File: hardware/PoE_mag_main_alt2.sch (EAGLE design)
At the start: 121 parts, among them IC1 LD1117S33TR, IC10 PCA9517A, IC2 DS1338, IC3 74LVC1T45SOT23-HAND, IC4 ATMEGA1284, IC5 MCP2200, IC6 TSR 1-2450, IC7 74LVC1T45SOT23-HAND, IC8 74LVC1T45SOT23-HAND, IC9 74LVC1T45SOT23-HAND, Q1 BSS138, Q3 BUK98150-55A, X1 PWR, X2 JTAG, X3 USB, X4 CONN-SMATHD, X5 UFL, X6 MICRO-SD-SOCKETHIROSE-DM3D, X7 RJ45, X8 RJ11, X9 22-23-2021, Y1 32k768, Y2 16MHz, Y3 12MHz

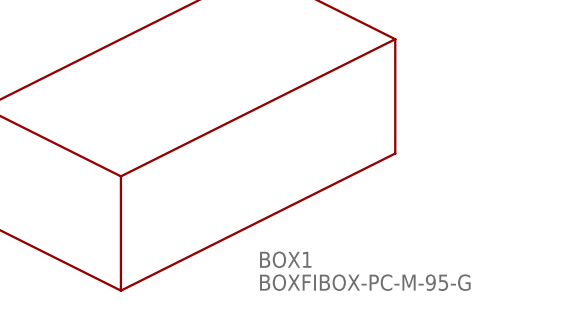
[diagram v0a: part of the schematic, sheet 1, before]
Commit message: Update enclosure outline
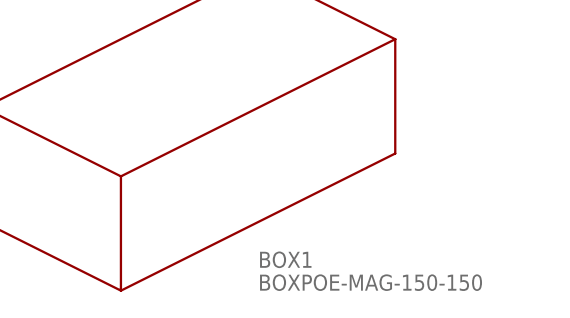
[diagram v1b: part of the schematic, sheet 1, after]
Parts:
- BOX1: value BOXFIBOX-PC-M-95-G -> BOXPOE-MAG-150-150; device fibox:BOXFIBOX-PC-M-95-G -> fibox:BOXPOE-MAG-150-150
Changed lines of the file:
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@@
 <grid distance="0.1" unitdist="inch" unit="inch" style="lines" multiple="1" display="no" altdistance="0.01" altunitdist="inch" altunit="inch"/>
 <layers>
-<layer number="1" name="Top" color="4" fill="1" visible="no" active="no"/>
-<layer number="2" name="Route2" color="1" fill="3" visible="no" active="no"/>
-<layer number="3" name="Route3" color="4" fill="3" visible="no" active="no"/>
-<layer number="14" name="Route14" color="1" fill="6" visible="no" active="no"/>
-<layer number="15" name="Route15" color="4" fill="6" visible="no" active="no"/>
-<layer number="16" name="Bottom" color="1" fill="1" visible="no" active="no"/>
-<layer number="17" name="Pads" color="2" fill="1" visible="no" active="no"/>
-<layer number="18" name="Vias" color="2" fill="1" visible="no" active="no"/>
-<layer number="19" name="Unrouted" color="6" fill="1" visible="no" active="no"/>
-<layer number="20" name="Dimension" color="15" fill="1" visible="no" active="no"/>
-<layer number="21" name="tPlace" color="7" fill="1" visible="no" active="no"/>
-<layer number="22" name="bPlace" color="7" fill="1" visible="no" active="no"/>
-<layer number="23" name="tOrigins" color="15" fill="1" visible="no" active="no"/>
-<layer number="24" name="bOrigins" color="15" fill="1" visible="no" active="no"/>
-<layer number="25" name="tNames" color="7" fill="1" visible="no" active="no"/>
-<layer number="26" name="bNames" color="7" fill="1" visible="no" active="no"/>
-<layer number="27" name="tValues" color="7" fill="1" visible="no" active="no"/>
-<layer number="28" name="bValues" color="7" fill="1" visible="no" active="no"/>
+<layer number="1" name="Top" color="4" fill="1" visible="yes" active="no"/>
+<layer number="2" name="Route2" color="1" fill="3" visible="yes" active="no"/>
+<layer number="3" name="Route3" color="4" fill="3" visible="yes" active="no"/>
+<layer number="14" name="Route14" color="1" fill="6" visible="yes" active="no"/>
+<layer number="15" name="Route15" color="4" fill="6" visible="yes" active="no"/>
+<layer number="16" name="Bottom" color="1" fill="1" visible="yes" active="no"/>
+<layer number="17" name="Pads" color="2" fill="1" visible="yes" active="no"/>
+<layer number="18" name="Vias" color="2" fill="1" visible="yes" active="no"/>
+<layer number="19" name="Unrouted" color="6" fill="1" visible="yes" active="no"/>
+<layer number="20" name="Dimension" color="14" fill="1" visible="yes" active="no"/>
+<layer number="21" name="tPlace" color="7" fill="1" visible="yes" active="no"/>
+<layer number="22" name="bPlace" color="7" fill="1" visible="yes" active="no"/>
+<layer number="23" name="tOrigins" color="15" fill="1" visible="yes" active="no"/>
+<layer number="24" name="bOrigins" color="15" fill="1" visible="yes" active="no"/>
+<layer number="25" name="tNames" color="7" fill="1" visible="yes" active="no"/>
+<layer number="26" name="bNames" color="7" fill="1" visible="yes" active="no"/>
+<layer number="27" name="tValues" color="7" fill="1" visible="yes" active="no"/>
+<layer number="28" name="bValues" color="7" fill="1" visible="yes" active="no"/>
 <layer number="29" name="tStop" color="7" fill="3" visible="no" active="no"/>
 <layer number="30" name="bStop" color="7" fill="6" visible="no" active="no"/>
@@
 <layer number="35" name="tGlue" color="7" fill="4" visible="no" active="no"/>
 <layer number="36" name="bGlue" color="7" fill="5" visible="no" active="no"/>
-<layer number="37" name="tTest" color="7" fill="1" visible="no" active="no"/>
-<layer number="38" name="bTest" color="7" fill="1" visible="no" active="no"/>
+<layer number="37" name="tTest" color="7" fill="1" visible="yes" active="no"/>
+<layer number="38" name="bTest" color="7" fill="1" visible="yes" active="no"/>
 <layer number="39" name="tKeepout" color="4" fill="11" visible="no" active="no"/>
 <layer number="40" name="bKeepout" color="1" fill="11" visible="no" active="no"/>
@@
 <layer number="44" name="Drills" color="7" fill="1" visible="no" active="no"/>
 <layer number="45" name="Holes" color="7" fill="1" visible="no" active="no"/>
-<layer number="46" name="Milling" color="3" fill="1" visible="no" active="no"/>
-<layer number="47" name="Measures" color="7" fill="1" visible="no" active="no"/>
-<layer number="48" name="Document" color="7" fill="1" visible="no" active="no"/>
-<layer number="49" name="Reference" color="7" fill="1" visible="no" active="no"/>
-<layer number="50" name="dxf" color="7" fill="1" visible="no" active="no"/>
-<layer number="51" name="tDocu" color="7" fill="1" visible="no" active="no"/>
-<layer number="52" name="bDocu" color="7" fill="1" visible="no" active="no"/>
-<layer number="53" name="tGND_GNDA" color="7" fill="9" visible="no" active="no"/>
-<layer number="54" name="bGND_GNDA" color="1" fill="9" visible="no" active="no"/>
-<layer number="56" name="wert" color="7" fill="1" visible="no" active="no"/>
-<layer number="57" name="tCAD" color="7" fill="1" visible="no" active="no"/>
+<layer number="46" name="Milling" color="3" fill="1" visible="yes" active="no"/>
+<layer number="47" name="Measures" color="7" fill="1" visible="yes" active="no"/>
+<layer number="48" name="Document" color="7" fill="1" visible="yes" active="no"/>
+<layer number="49" name="Reference" color="7" fill="1" visible="yes" active="no"/>
+<layer number="50" name="dxf" color="7" fill="1" visible="yes" active="no"/>
+<layer number="51" name="tDocu" color="7" fill="1" visible="yes" active="no"/>
+<layer number="52" name="bDocu" color="7" fill="1" visible="yes" active="no"/>
+<layer number="53" name="tGND_GNDA" color="7" fill="9" visible="yes" active="no"/>
+<layer number="54" name="bGND_GNDA" color="1" fill="9" visible="yes" active="no"/>
+<layer number="56" name="wert" color="7" fill="1" visible="yes" active="no"/>
+<layer number="57" name="tCAD" color="7" fill="1" visible="yes" active="no"/>
 <layer number="91" name="Nets" color="2" fill="1" visible="yes" active="yes"/>
 <layer number="92" name="Busses" color="1" fill="1" visible="yes" active="yes"/>
@@
 <part name="GND48" library="supply1" deviceset="GND" device=""/>
 <part name="X9" library="con-molex" deviceset="22-23-2021" device=""/>
-<part name="BOX1" library="fibox" deviceset="BOX" device="FIBOX-PC-M-95-G"/>
+<part name="BOX1" library="fibox" deviceset="BOX" device="POE-MAG-150-150" value="BOXPOE-MAG-150-150"/>
 <part name="Q3" library="SteveMarple" deviceset="FET-N-TYPE" device="SOT223-HAND" value="BUK98150-55A"/>
 </parts>

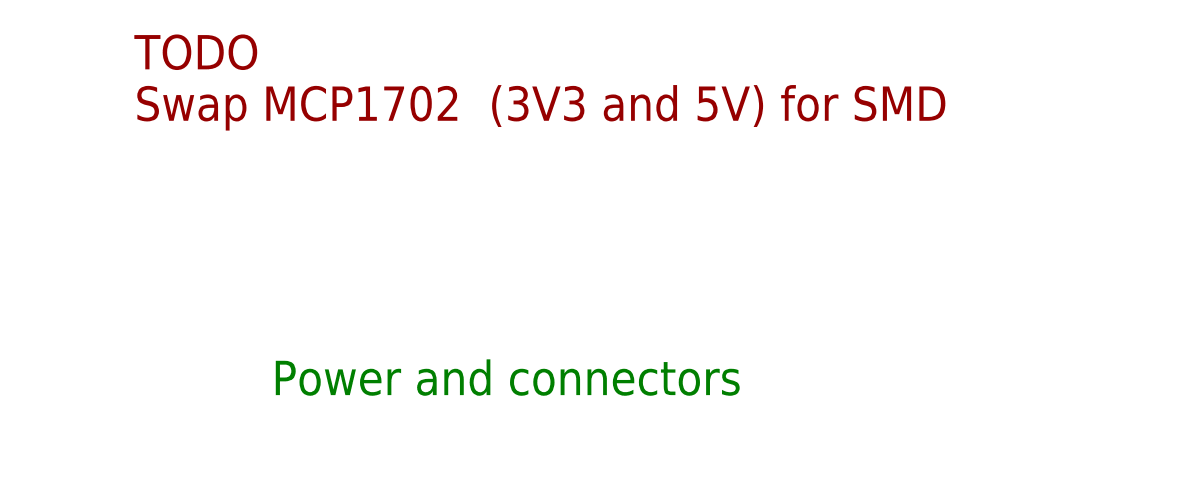
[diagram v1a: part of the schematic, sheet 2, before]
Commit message: Update enclosure restrictions
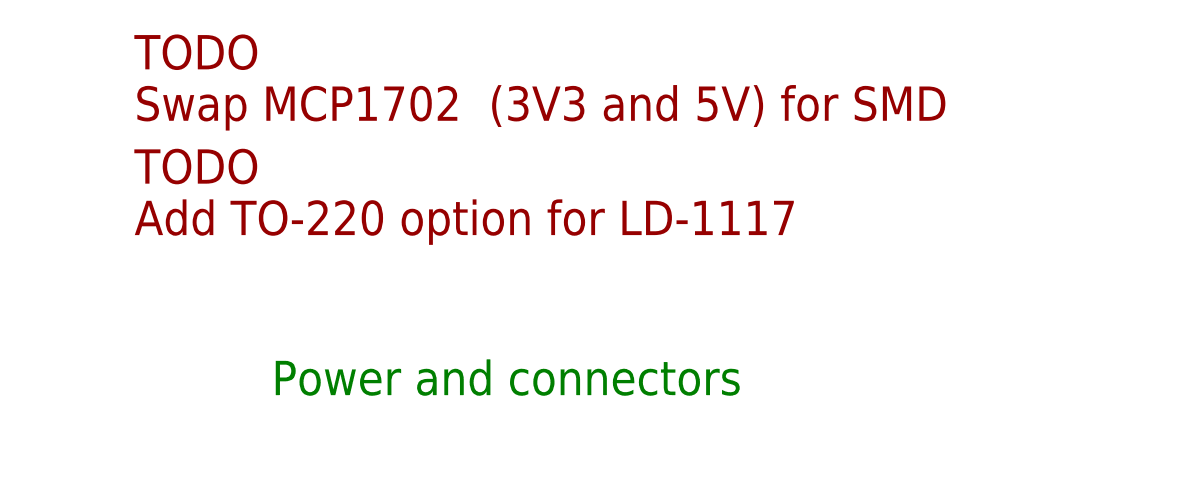
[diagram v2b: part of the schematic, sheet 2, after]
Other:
- note added: "TODO Add TO-220 option for LD-1117"
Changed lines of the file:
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@@
 <text x="-149.86" y="200.66" size="3.81" layer="94">TODO
 Swap MCP1702  (3V3 and 5V) for SMD</text>
+<text x="-149.86" y="187.96" size="3.81" layer="94">TODO
+Add TO-220 option for LD-1117</text>
 </plain>
 <instances>

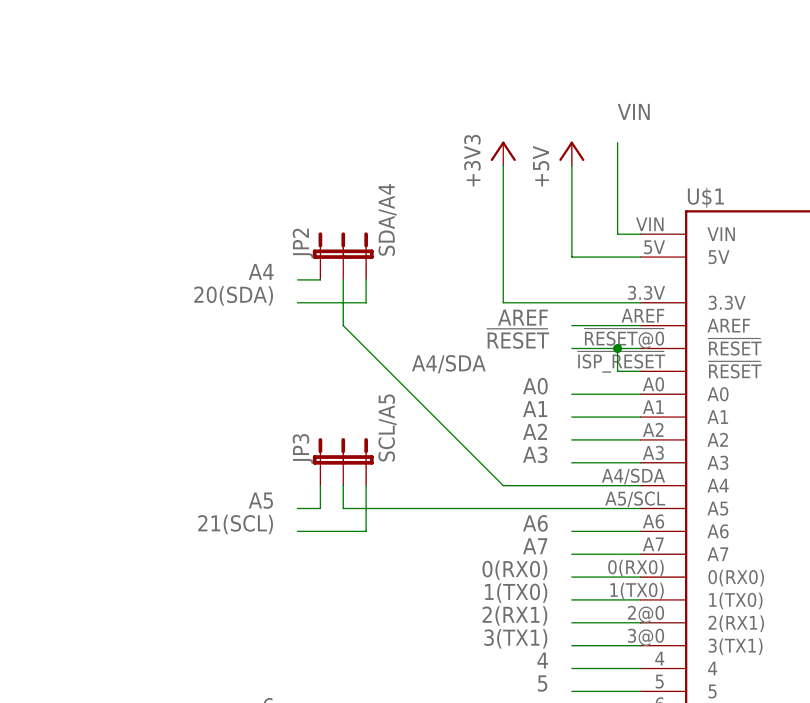
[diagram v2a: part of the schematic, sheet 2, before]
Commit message: Fix silkscreen text
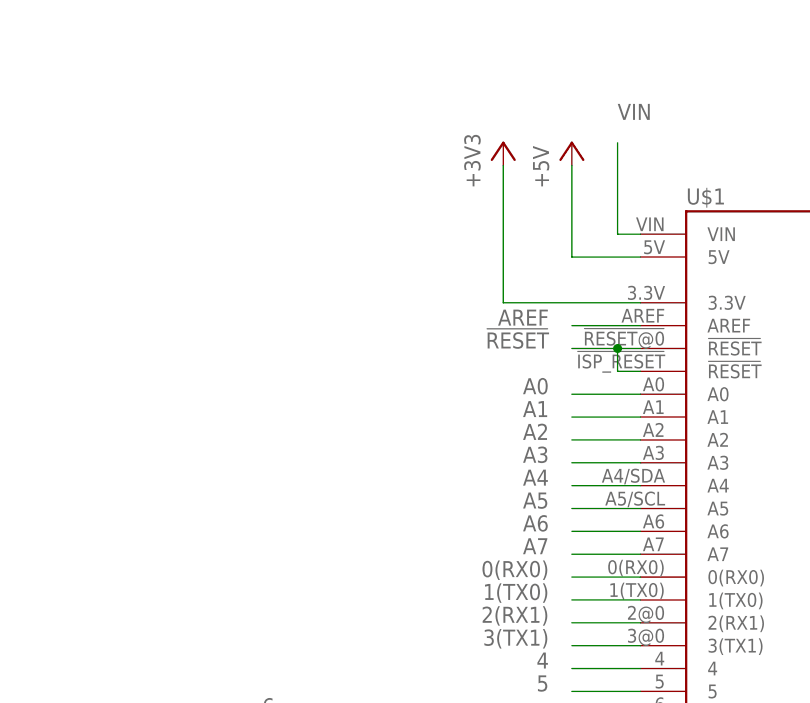
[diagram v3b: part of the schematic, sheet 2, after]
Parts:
- removed JP2: SDA/A4, SparkFun:JUMPER-3PTH
- removed JP3: SCL/A5, SparkFun:JUMPER-3PTH
- JP4: value PPS 7/6 -> PPS
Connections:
- net N$16 renamed VBUS
- removed net A4/SDA: JP2.2, U$1.A4
- removed net A5/SCL: JP3.2, U$1.A5
- net 20(SDA): no longer JP2.3
- net 21(SCL): no longer JP3.3
- net A4: now also U$1.A4; no longer JP2.1
- net A5: now also U$1.A5; no longer JP3.1
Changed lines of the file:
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@@
 <part name="Y1" library="SteveMarple" deviceset="CRYSTAL" device="TC38H" value="32k768"/>
 <part name="R2" library="SteveMarple" deviceset="RESISTOR" device="1206-HAND" value="560R"/>
-<part name="JP2" library="SparkFun" deviceset="JUMPER-3" device="PTH" value="SDA/A4"/>
-<part name="JP3" library="SparkFun" deviceset="JUMPER-3" device="PTH" value="SCL/A5"/>
 <part name="R6" library="SteveMarple" deviceset="RESISTOR" device="1206-HAND" value="10k"/>
 <part name="SENS1" library="SteveMarple" deviceset="LM61" device=""/>
@@
 <part name="R11" library="SteveMarple" deviceset="RESISTOR" device="1206-HAND" value="10k"/>
 <part name="IC9" library="SteveMarple" deviceset="74LVC1T45" device="SOT23-HAND"/>
-<part name="JP4" library="SparkFun" deviceset="JUMPER-3" device="PTH" value="PPS 7/6"/>
+<part name="JP4" library="SparkFun" deviceset="JUMPER-3" device="PTH" value="PPS"/>
 <part name="R12" library="SteveMarple" deviceset="RESISTOR" device="1206-HAND" value="100k"/>
 <part name="GND33" library="supply1" deviceset="GND" device=""/>
@@
 </instance>
 <instance part="R2" gate="G$1" x="137.16" y="132.08" rot="R90"/>
-<instance part="JP2" gate="G$1" x="-22.86" y="154.94"/>
-<instance part="JP3" gate="G$1" x="-22.86" y="132.08"/>
 <instance part="R6" gate="G$1" x="-149.86" y="68.58" rot="R90"/>
 <instance part="SENS1" gate="G$1" x="149.86" y="0" rot="MR0"/>
@@
 </segment>
 </net>
-<net name="A4/SDA" class="0">
-<segment>
-<wire x1="-2.54" y1="129.54" x2="-20.32" y2="147.32" width="0.1524" layer="91"/>
-<wire x1="-20.32" y1="147.32" x2="-20.32" y2="152.4" width="0.1524" layer="91"/>
-<pinref part="JP2" gate="G$1" pin="2"/>
-<label x="-12.7" y="142.24" size="1.778" layer="95"/>
-<pinref part="U$1" gate="G$1" pin="A4"/>
-<wire x1="-2.54" y1="129.54" x2="12.7" y2="129.54" width="0.1524" layer="91"/>
-</segment>
-</net>
-<net name="A5/SCL" class="0">
-<segment>
-<wire x1="12.7" y1="127" x2="-20.32" y2="127" width="0.1524" layer="91"/>
-<wire x1="-20.32" y1="127" x2="-20.32" y2="129.54" width="0.1524" layer="91"/>
-<pinref part="JP3" gate="G$1" pin="2"/>
-<pinref part="U$1" gate="G$1" pin="A5"/>
-</segment>
-</net>
 <net name="20(SDA)" class="0">
-<segment>
-<wire x1="-17.78" y1="152.4" x2="-17.78" y2="149.86" width="0.1524" layer="91"/>
-<wire x1="-17.78" y1="149.86" x2="-25.4" y2="149.86" width="0.1524" layer="91"/>
-<label x="-27.94" y="149.86" size="1.778" layer="95" rot="MR0"/>
-<pinref part="JP2" gate="G$1" pin="3"/>
-</segment>
 <segment>
 <wire x1="152.4" y1="63.5" x2="185.42" y2="63.5" width="0.1524" layer="91"/>
@@
 <net name="21(SCL)" class="0">
 <segment>
-<wire x1="-17.78" y1="129.54" x2="-17.78" y2="124.46" width="0.1524" layer="91"/>
-<wire x1="-17.78" y1="124.46" x2="-25.4" y2="124.46" width="0.1524" layer="91"/>
-<label x="-27.94" y="124.46" size="1.778" layer="95" rot="MR0"/>
-<pinref part="JP3" gate="G$1" pin="3"/>
-</segment>
-<segment>
 <wire x1="152.4" y1="66.04" x2="177.8" y2="66.04" width="0.1524" layer="91"/>
 <wire x1="177.8" y1="66.04" x2="187.96" y2="66.04" width="0.1524" layer="91"/>
@@
 <net name="A4" class="0">
 <segment>
-<wire x1="-22.86" y1="152.4" x2="-25.4" y2="152.4" width="0.1524" layer="91"/>
-<label x="-27.94" y="152.4" size="1.778" layer="95" rot="MR0"/>
-<pinref part="JP2" gate="G$1" pin="1"/>
-</segment>
-<segment>
 <wire x1="53.34" y1="50.8" x2="55.88" y2="50.8" width="0.1524" layer="91"/>
 <label x="58.42" y="50.8" size="1.778" layer="95"/>
 <pinref part="IC4" gate="G$1" pin="PCINT3/ADC3_PA3"/>
 </segment>
+<segment>
+<label x="2.54" y="129.54" size="1.778" layer="95" rot="MR0"/>
+<pinref part="U$1" gate="G$1" pin="A4"/>
+<wire x1="5.08" y1="129.54" x2="12.7" y2="129.54" width="0.1524" layer="91"/>
+</segment>
 </net>
 <net name="A5" class="0">
-<segment>
-<wire x1="-22.86" y1="129.54" x2="-22.86" y2="127" width="0.1524" layer="91"/>
-<wire x1="-22.86" y1="127" x2="-25.4" y2="127" width="0.1524" layer="91"/>
-<label x="-27.94" y="127" size="1.778" layer="95" rot="MR0"/>
-<pinref part="JP3" gate="G$1" pin="1"/>
-</segment>
 <segment>
 <wire x1="53.34" y1="53.34" x2="55.88" y2="53.34" width="0.1524" layer="91"/>
 <label x="58.42" y="53.34" size="1.778" layer="95"/>
 <pinref part="IC4" gate="G$1" pin="PCINT2/ADC2_PA2"/>
+</segment>
+<segment>
+<wire x1="12.7" y1="127" x2="5.08" y2="127" width="0.1524" layer="91"/>
+<pinref part="U$1" gate="G$1" pin="A5"/>
+<label x="2.54" y="127" size="1.778" layer="95" rot="MR0"/>
 </segment>
 </net>
@@
 </segment>
 </net>
-<net name="N$16" class="1">
+<net name="VBUS" class="1">
 <segment>
 <pinref part="X3" gate="G$1" pin="VBUS"/>

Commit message: Use TO220 package of LD1117
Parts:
- IC1: device SteveMarple:V_REG_LD1117VXXSOT223-HAND -> SteveMarple:V_REG_LD1117VXXTO220
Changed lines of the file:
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@@
 <part name="IC6" library="SteveMarple" deviceset="V_REG_78XX" device="TSR-1-XXXX" value="TSR 1-2450"/>
 <part name="JP9" library="SparkFun" deviceset="JUMPER-3" device="PTH" value="USB/VIN"/>
-<part name="IC1" library="SteveMarple" deviceset="V_REG_LD1117VXX" device="SOT223-HAND" value="LD1117S33TR"/>
+<part name="IC1" library="SteveMarple" deviceset="V_REG_LD1117VXX" device="TO220" value="LD1117S33TR"/>
 <part name="FRAME3" library="SteveMarple" deviceset="FRAME-A3" device=""/>
 <part name="RF1" library="nvs-tech" deviceset="NV08C-CSM" device="HAND" value="NV08C-CSM"/>
